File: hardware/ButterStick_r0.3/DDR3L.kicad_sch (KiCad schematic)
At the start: 7 parts, among them U8 MT41K64M16TW-107_J-TR

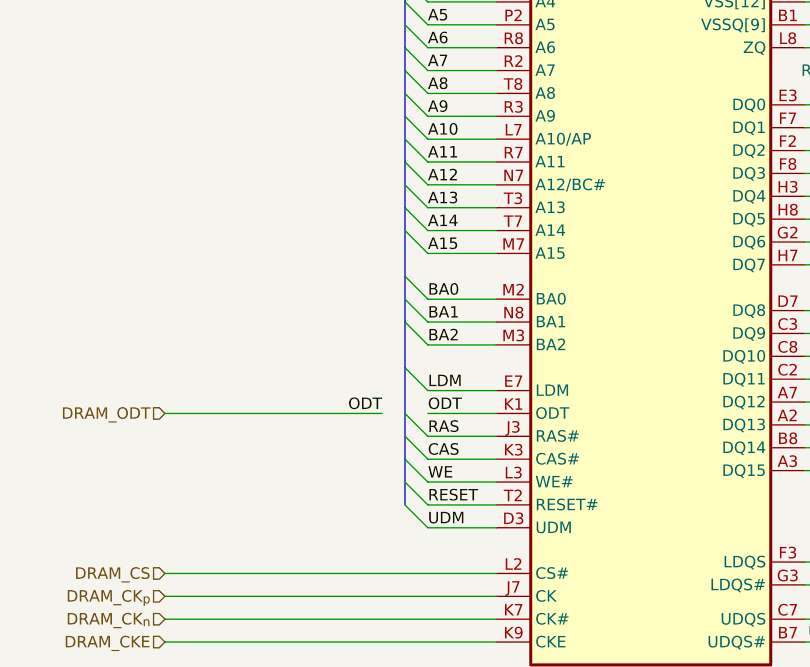
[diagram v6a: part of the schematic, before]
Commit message: hw.r0d3: update routing
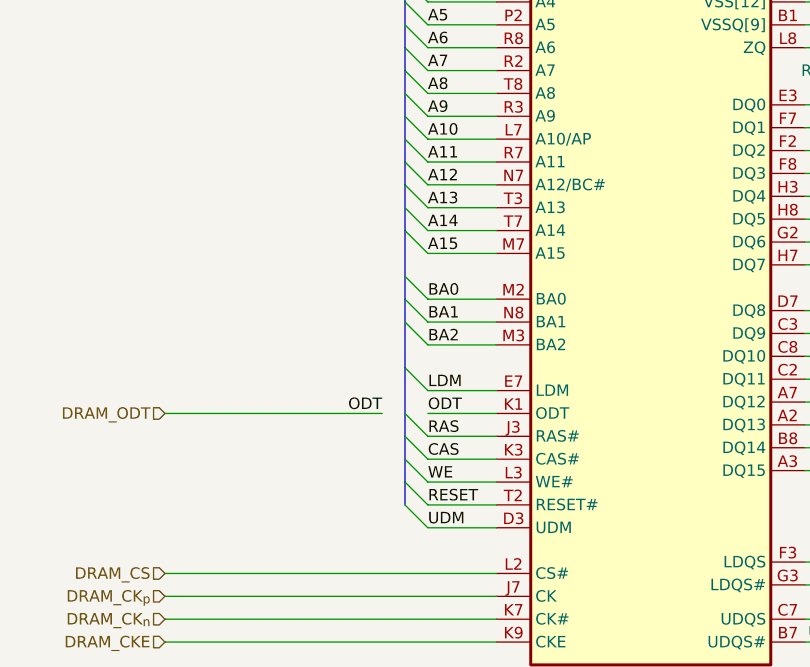
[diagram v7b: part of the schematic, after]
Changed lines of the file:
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@@
 (kicad_sch (version 20200608) (host eeschema "5.99.0-unknown-08c61e6~101~ubuntu18.04.1")
-  (page 14 19)
+  (page 1 19)
   (paper "A4")
   (junction (at 134.62 35.56))
@@
     (stroke (width 0) (type solid) (color 0 0 0 0))
   )
-  (bus (pts (xy 110.49 93.98) (xy 110.49 99.06))
-    (stroke (width 0) (type solid) (color 0 0 0 0))
-  )
-  (bus (pts (xy 110.49 99.06) (xy 110.49 106.68))
-    (stroke (width 0) (type solid) (color 0 0 0 0))
-  )
-  (bus (pts (xy 110.49 106.68) (xy 110.49 111.76))
-    (stroke (width 0) (type solid) (color 0 0 0 0))
-  )
-  (bus (pts (xy 110.49 111.76) (xy 110.49 116.84))
+  (bus (pts (xy 110.49 93.98) (xy 110.49 96.52))
+    (stroke (width 0) (type solid) (color 0 0 0 0))
+  )
+  (bus (pts (xy 110.49 96.52) (xy 110.49 101.6))
+    (stroke (width 0) (type solid) (color 0 0 0 0))
+  )
+  (bus (pts (xy 110.49 101.6) (xy 110.49 109.22))
+    (stroke (width 0) (type solid) (color 0 0 0 0))
+  )
+  (bus (pts (xy 110.49 109.22) (xy 110.49 116.84))
     (stroke (width 0) (type solid) (color 0 0 0 0))
   )
@@
     (stroke (width 0) (type solid) (color 0 0 0 0))
   )
-  (bus (pts (xy 110.49 124.46) (xy 110.49 127))
-    (stroke (width 0) (type solid) (color 0 0 0 0))
-  )
-  (bus (pts (xy 110.49 127) (xy 110.49 132.08))
-    (stroke (width 0) (type solid) (color 0 0 0 0))
-  )
+  (bus (pts (xy 110.49 124.46) (xy 110.49 129.54))
+    (stroke (width 0) (type solid) (color 0 0 0 0))
+  )
+  (bus (pts (xy 110.49 129.54) (xy 110.49 132.08))
+    (stroke (width 0) (type solid) (color 0 0 0 0))
+  )

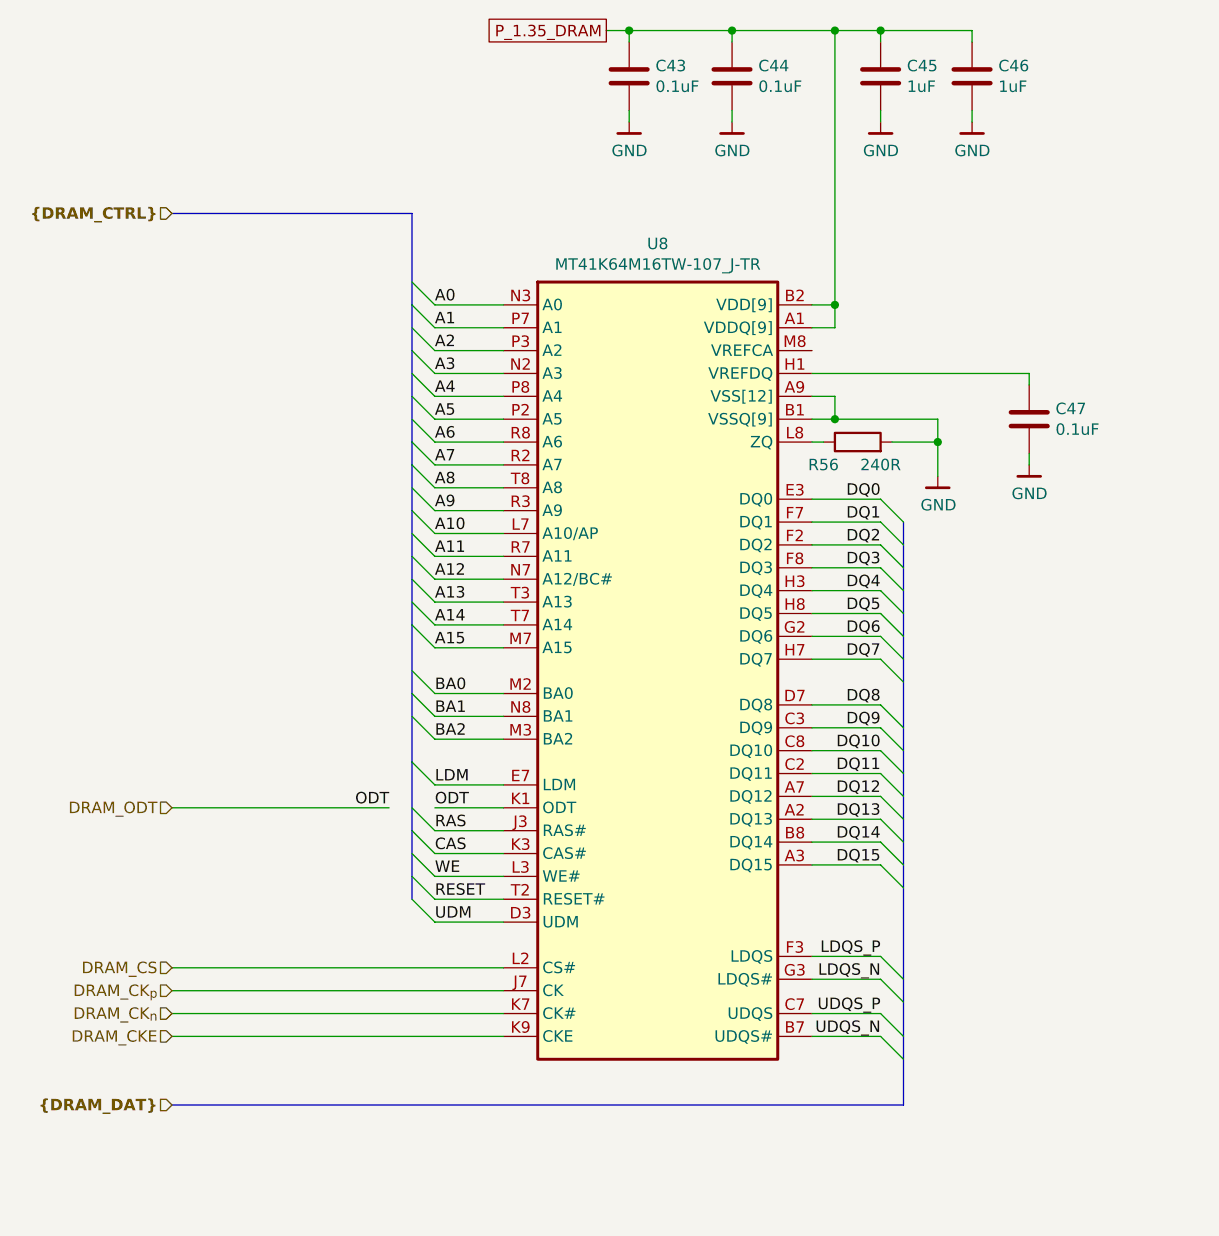
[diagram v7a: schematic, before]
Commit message: hw.r0d3: Continue routing
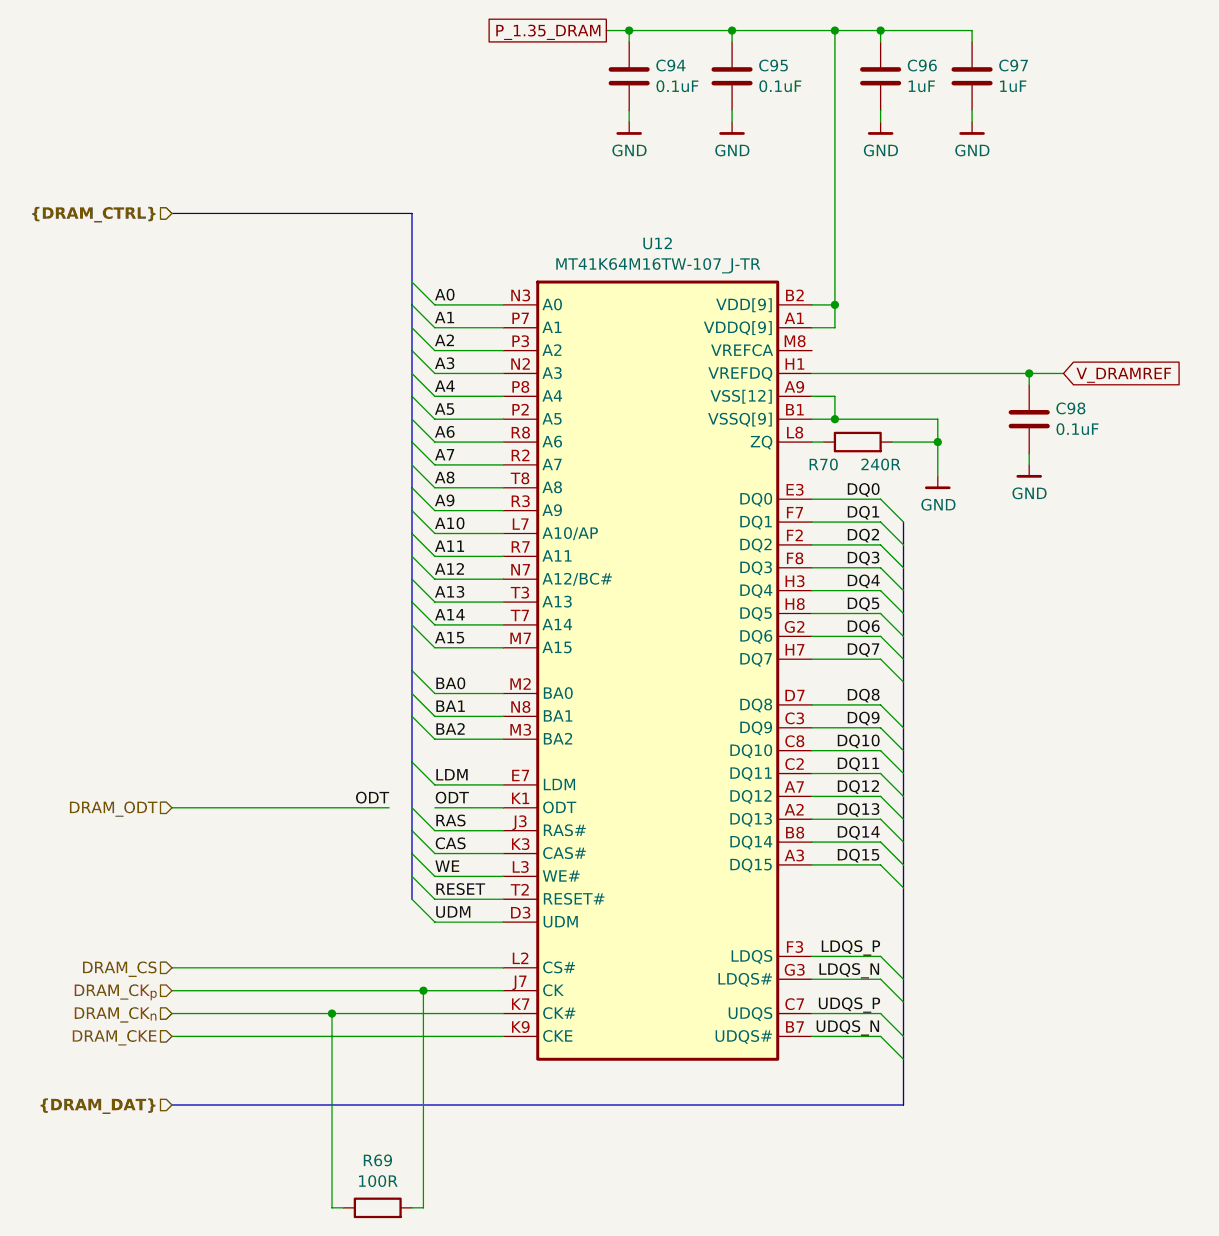
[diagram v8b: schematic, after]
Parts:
- added R69: 100R, Resistor_SMD:R_0402_1005Metric, symbol Device:R
- renumbered C43 to C94, C44 to C95, C45 to C96, C46 to C97, C47 to C98, R56 to R70, U8 to U12
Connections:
- net DRAM_CK_{n}: now also R69.1
- net DRAM_CK_{p}: now also R69.2
- net V_DRAMREF: now reaches C98.1, U12.H1 (VREFDQ)
